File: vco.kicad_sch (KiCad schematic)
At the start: 122 parts, among them J1 EXP FM, J10 Square, J11 Conn_02x05_Odd_Even, J2 1V/OCT, J3 1V/OCT, J4 LIN FM, J5 PWM, J6 SYNC, J7 Sine, J8 Saw, J9 Triangle, Q1 MMBFJ111, SW1 Sync Mode, U1 TL074, U2 OPA2134, U3 L78L12_SO8, U4 L79L12_SO8, U5 thermally_coupled_transistor_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, U6 TL074, U7 LM311

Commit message: checking all resistor values
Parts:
- RV11: value 220K -> 47K
- RV9: value 220K -> 10K
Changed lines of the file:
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@@
     (in_bom yes) (on_board yes) (fields_autoplaced)
     (property "Reference" "RV9" (id 0) (at 182.88 119.8864 90))
-    (property "Value" "220K" (id 1) (at 182.88 122.4233 90))
+    (property "Value" "10K" (id 1) (at 182.88 122.4233 90))
     (property "Footprint" "Potentiometer_THT:Potentiometer_Bourns_3296W_Vertical" (id 2) (at 182.88 116.84 0)
       (effects (font (size 1.27 1.27)) hide)
@@
     (in_bom yes) (on_board yes) (fields_autoplaced)
     (property "Reference" "RV11" (id 0) (at 265.43 13.0642 90))
-    (property "Value" "220K" (id 1) (at 265.43 15.6011 90))
+    (property "Value" "47K" (id 1) (at 265.43 15.6011 90))
     (property "Footprint" "Potentiometer_THT:Potentiometer_Bourns_3296W_Vertical" (id 2) (at 265.43 17.78 0)
       (effects (font (size 1.27 1.27)) hide)
@@
     )
     (path "/58d5e9aa-5595-4f3e-9fc6-52cb927712d1"
-      (reference "RV9") (unit 1) (value "220K") (footprint "Potentiometer_THT:Potentiometer_Bourns_3296W_Vertical")
+      (reference "RV9") (unit 1) (value "10K") (footprint "Potentiometer_THT:Potentiometer_Bourns_3296W_Vertical")
     )
     (path "/37fdaf0a-cf60-456d-b11f-b915c1ec581e"
@@
     )
     (path "/a99e6af1-8dcb-42e4-b924-4b2e7e354e65"
-      (reference "RV11") (unit 1) (value "220K") (footprint "Potentiometer_THT:Potentiometer_Bourns_3296W_Vertical")
+      (reference "RV11") (unit 1) (value "47K") (footprint "Potentiometer_THT:Potentiometer_Bourns_3296W_Vertical")
     )
     (path "/a04003e4-c542-4884-a43e-7ae3c8ee89d5"

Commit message: v2 ready for manu
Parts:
- added D7, D8: D_Dual_Series_AKC, Package_TO_SOT_SMD:SOT-23_Handsoldering, symbol Device:D_Dual_Series_AKC
- D1, D2, D3, D4, D5, D6: footprint Diode_SMD:D_SOD-323 -> Diode_SMD:D_SOD-323_HandSoldering
- H1: value 1V/OCT -> 1v/oct; symbol Mechanical:MountingHole -> Mechanical:MountingHole_Pad; now left out of the parts list
- H10: value MountingHole -> square; footprint (none) -> Eurorack:Mech-AudioJack-Hole-Output; symbol Mechanical:MountingHole -> Eurorack:MountingHole_Pad_Output; now left out of the parts list
- H11: value MountingHole -> frequency; footprint (none) -> Eurorack:Mech-Potentiometer-Hole_level; symbol Mechanical:MountingHole -> Mechanical:MountingHole_Pad; now left out of the parts list
- H12: value MountingHole -> fine tune; footprint (none) -> Eurorack:Mech-Potentiometer-Hole_pan; symbol Mechanical:MountingHole -> Mechanical:MountingHole_Pad; now left out of the parts list
- H13: value MountingHole -> lin fm; footprint (none) -> Eurorack:Mech-Potentiometer-Hole_level; symbol Mechanical:MountingHole -> Mechanical:MountingHole_Pad; now left out of the parts list
- H14: value MountingHole -> exp fm; footprint (none) -> Eurorack:Mech-Potentiometer-Hole_level; symbol Mechanical:MountingHole -> Mechanical:MountingHole_Pad; now left out of the parts list
- H15: value MountingHole -> pw; footprint (none) -> Eurorack:Mech-Potentiometer-Hole_pan; symbol Mechanical:MountingHole -> Mechanical:MountingHole_Pad; now left out of the parts list
- H16: value MountingHole -> pwm lvl; footprint (none) -> Eurorack:Mech-Potentiometer-Hole_level; symbol Mechanical:MountingHole -> Mechanical:MountingHole_Pad; now left out of the parts list
- H17: footprint (none) -> Eurorack:Mech-MountingHole; symbol Mechanical:MountingHole -> Mechanical:MountingHole_Pad; now left out of the parts list
- H18, H19, H20: symbol Mechanical:MountingHole -> Mechanical:MountingHole_Pad; now left out of the parts list
- H2: value MountingHole -> 1v/oct; footprint (none) -> Eurorack:Mech-AudioJack-Hole; symbol Mechanical:MountingHole -> Mechanical:MountingHole_Pad; now left out of the parts list
- H21: value MountingHole -> sync hardness; footprint (none) -> Eurorack:Mech-2M_Switch-Hole; symbol Mechanical:MountingHole -> Mechanical:MountingHole_Pad; now left out of the parts list
- H3: value MountingHole -> exp fm; footprint (none) -> Eurorack:Mech-AudioJack-Hole; symbol Mechanical:MountingHole -> Mechanical:MountingHole_Pad; now left out of the parts list
- H4: value MountingHole -> lin fm; footprint (none) -> Eurorack:Mech-AudioJack-Hole; symbol Mechanical:MountingHole -> Mechanical:MountingHole_Pad; now left out of the parts list
- H5: value MountingHole -> pwm; footprint (none) -> Eurorack:Mech-AudioJack-Hole; symbol Mechanical:MountingHole -> Mechanical:MountingHole_Pad; now left out of the parts list
- H6: value MountingHole -> sync; footprint (none) -> Eurorack:Mech-AudioJack-Hole; symbol Mechanical:MountingHole -> Mechanical:MountingHole_Pad; now left out of the parts list
- H7: value MountingHole -> sine; footprint (none) -> Eurorack:Mech-AudioJack-Hole-Output; symbol Mechanical:MountingHole -> Mechanical:MountingHole_Pad; now left out of the parts list
- H8: value MountingHole -> triangle; footprint (none) -> Eurorack:Mech-AudioJack-Hole-Output; symbol Mechanical:MountingHole -> Mechanical:MountingHole_Pad; now left out of the parts list
- H9: value MountingHole -> saw; footprint (none) -> Eurorack:Mech-AudioJack-Hole-Output; symbol Mechanical:MountingHole -> Mechanical:MountingHole_Pad; now left out of the parts list
- J1, J10, J2, J3, J4, J5, J6, J7, J8, J9: symbol Connector:AudioJack2_SwitchT -> Connector_Audio:AudioJack2_SwitchT; PartNum (none) -> A-2566; Vendor (none) -> Tayda
- J11: PartNum (none) -> A-2939; Vendor (none) -> Tayda
- Q1: PartNum (none) -> 512-MMBFJ111; Vendor (none) -> Mouser
- RV1: value EXP FM LVL -> B25K; PartNum (none) -> A-2491; Vendor (none) -> Tayda
- RV10: PartNum (none) -> A-587; Vendor (none) -> Tayda
- RV11: PartNum (none) -> A-598; Vendor (none) -> Tayda
- RV2: value LIN FM LVL -> B25K; PartNum (none) -> A-2491; Vendor (none) -> Tayda
- RV3: value PWM LVL -> B25K; PartNum (none) -> A-2491; Vendor (none) -> Tayda
- RV4: value Tune -> B25K; PartNum (none) -> A-2491; Vendor (none) -> Tayda
- RV5: value Fine Tune -> B25K; PartNum (none) -> A-2491; Vendor (none) -> Tayda
- RV6: PartNum (none) -> A-310; Vendor (none) -> Tayda
- RV7: value PW -> B25K; PartNum (none) -> A-2491; Vendor (none) -> Tayda
- RV8: PartNum (none) -> A-595; Vendor (none) -> Tayda
- RV9: PartNum (none) -> A-586; Vendor (none) -> Tayda
- SW1: PartNum (none) -> X-4673; Vendor (none) -> Tayda
- U1: PartNum (none) -> 595-TL074CN; Vendor (none) -> Mouser
- U2: PartNum (none) -> 595-OPA2137UA/2K5 --or-- 595-OPA2134UA/2K5; Vendor (none) -> Mouser
- U3: PartNum (none) -> 863-NCV78L12ABDR2G; Vendor (none) -> Mouser
- U4: PartNum (none) -> 863-MC79L12ABDR2G; Vendor (none) -> Mouser
- U5: PartNum (none) -> 771-BCM847DS135 --and-- LT16S102F33; Vendor (none) -> Mouser --and-- Thonk
- U6: PartNum (none) -> 595-TL074CDR; Vendor (none) -> Mouser
- U7: PartNum (none) -> 863-LM311DR2G; Vendor (none) -> Mouser
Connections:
- net GND: now also U6.12 (+); no longer U1.12 (+)
- net at D3.1 (K), R30.1, R35.1: now also U6.13 (-); no longer U1.13 (-)
- net at R12.2, U3.8 (IN): now also D7.2 (K), D8.2 (K); no longer J11.10 (Pin_10), J11.9 (Pin_9)
- net at R31.2, R32.2, R34.2: now also U1.12 (+); no longer U6.12 (+)
- net at R33.1: now also U1.13 (-); no longer U6.13 (-)
- net at U6.14: now also D3.2 (A), D4.1 (K); no longer R39.2
- net at R13.1, U4.2 (IN), U4.3 (IN)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: now also D7.1 (A), D8.1 (A); no longer J11.1 (Pin_1), J11.2 (Pin_2)
- new net: D8.3 (common), J11.1 (Pin_1), J11.2 (Pin_2)
- new net: D7.3 (common), J11.10 (Pin_10), J11.9 (Pin_9)
- new net: R39.2, U1.14
- new net face: H1.1, H10.1, H11.1, H12.1, H13.1, H14.1, H15.1, H16.1, H17.1, H18.1, H19.1, H2.1, H20.1, H21.1, H3.1, H4.1, H5.1, H6.1, H7.1, H8.1, H9.1
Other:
- moved on the sheet: D6, J11, U1D, U6D

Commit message: wrong part number
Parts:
- SW1: PartNum X-4673 -> A-6087
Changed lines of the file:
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@@
       (effects (font (size 1.27 1.27)) hide)
     )
-    (property "PartNum" "X-4673" (at 52.07 116.84 0)
+    (property "PartNum" "A-6087" (at 52.07 116.84 0)
       (effects (font (size 1.27 1.27)) hide)
     )

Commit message: v2 just about ready for manu
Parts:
- D7, D8: footprint Package_TO_SOT_SMD:SOT-23_Handsoldering -> Package_TO_SOT_SMD:SOT-23
- H1, H2: footprint Eurorack:Mech-AudioJack-Hole -> Eurorack:Mech-AudioJack-Hole-Input-Voct
- H3, H4, H5: footprint Eurorack:Mech-AudioJack-Hole -> Eurorack:Mech-AudioJack-Hole-Input-CV
- H6: footprint Eurorack:Mech-AudioJack-Hole -> Eurorack:Mech-AudioJack-Hole-Input-Clock
- Q1: value MMBFJ111 -> MMBFJ113
- R40: value 4.7K -> 8.2K
- R45: value 200K -> 180K
- R49: value 1.5K -> 1.2K
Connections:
- net +12V: now also D7.2 (K), D8.2 (K), U3.8 (IN); no longer R12.1
- net -12V: now also D7.1 (A), D8.1 (A), U4.2 (IN), U4.3 (IN), U4.6 (IN), U4.7 (IN); no longer R13.2
- net at J11.1 (Pin_1), J11.2 (Pin_2): now also R13.2; no longer D8.3 (common)
- net at J11.10 (Pin_10), J11.9 (Pin_9): now also R12.1; no longer D7.3 (common)
- new net: D8.3 (common), R13.1
- new net: D7.3 (common), R12.2
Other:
- moved on the sheet: C10, C8, C9, R12, R13, U1E, U2C, U6E

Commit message: bom fixes
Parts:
- C2, C3: value 22U 50V -> 22u 50V
- R1: value 70K -> 68K
- R2, R38: value 50K -> 47K
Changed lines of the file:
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@@
   (symbol (lib_id "Device:C") (at 116.84 238.76 90) (unit 1)
     (in_bom yes) (on_board yes) (dnp no) (fields_autoplaced)
-    (property "Reference" "C3" (at 116.84 232.9012 90)
+    (property "Reference" "C3" (at 116.84 231.14 90)
       (effects (font (size 1.27 1.27)))
     )
-    (property "Value" "22U 50V" (at 116.84 235.4381 90)
+    (property "Value" "22u 50V" (at 116.84 233.68 90)
       (effects (font (size 1.27 1.27)))
     )
@@
   (symbol (lib_id "Device:R") (at 254 39.37 0) (unit 1)
     (in_bom yes) (on_board yes) (dnp no) (fields_autoplaced)
-    (property "Reference" "R38" (at 255.778 38.5353 0)
+    (property "Reference" "R38" (at 256.54 38.1 0)
       (effects (font (size 1.27 1.27)) (justify left))
     )
-    (property "Value" "50K" (at 255.778 41.0722 0)
+    (property "Value" "47K" (at 256.54 40.64 0)
       (effects (font (size 1.27 1.27)) (justify left))
     )
@@
   (symbol (lib_id "Device:C") (at 116.84 209.55 90) (unit 1)
     (in_bom yes) (on_board yes) (dnp no) (fields_autoplaced)
-    (property "Reference" "C2" (at 116.84 203.6912 90)
+    (property "Reference" "C2" (at 116.84 201.93 90)
       (effects (font (size 1.27 1.27)))
     )
-    (property "Value" "22U 50V" (at 116.84 206.2281 90)
+    (property "Value" "22u 50V" (at 116.84 204.47 90)
       (effects (font (size 1.27 1.27)))
     )
@@
   (symbol (lib_id "Device:R") (at 87.63 41.91 180) (unit 1)
     (in_bom yes) (on_board yes) (dnp no) (fields_autoplaced)
-    (property "Reference" "R1" (at 89.408 41.0753 0)
+    (property "Reference" "R1" (at 90.17 40.64 0)
       (effects (font (size 1.27 1.27)) (justify right))
     )
-    (property "Value" "70K" (at 89.408 43.6122 0)
+    (property "Value" "68K" (at 90.17 43.18 0)
       (effects (font (size 1.27 1.27)) (justify right))
     )
@@
   (symbol (lib_id "Device:R") (at 87.63 49.53 180) (unit 1)
     (in_bom yes) (on_board yes) (dnp no) (fields_autoplaced)
-    (property "Reference" "R2" (at 89.408 48.6953 0)
+    (property "Reference" "R2" (at 90.17 48.26 0)
       (effects (font (size 1.27 1.27)) (justify right))
     )
-    (property "Value" "50K" (at 89.408 51.2322 0)
+    (property "Value" "47K" (at 90.17 50.8 0)
       (effects (font (size 1.27 1.27)) (justify right))
     )

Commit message: more bom fixes
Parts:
- SW1: PartNum A-6087 -> A-5751
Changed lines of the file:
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@@
       (effects (font (size 1.27 1.27)) hide)
     )
-    (property "PartNum" "A-6087" (at 52.07 116.84 0)
+    (property "PartNum" "A-5751" (at 52.07 116.84 0)
       (effects (font (size 1.27 1.27)) hide)
     )

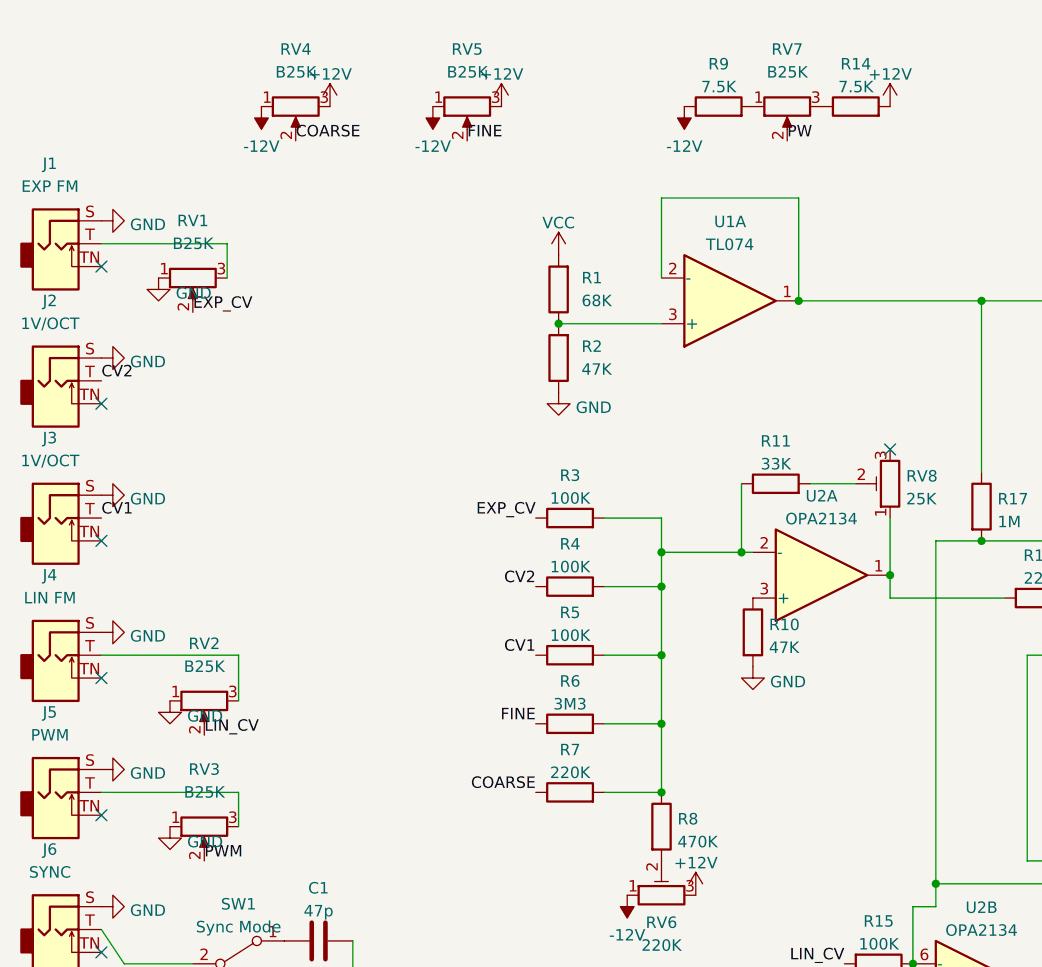
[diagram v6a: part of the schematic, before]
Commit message: more BOM fixes
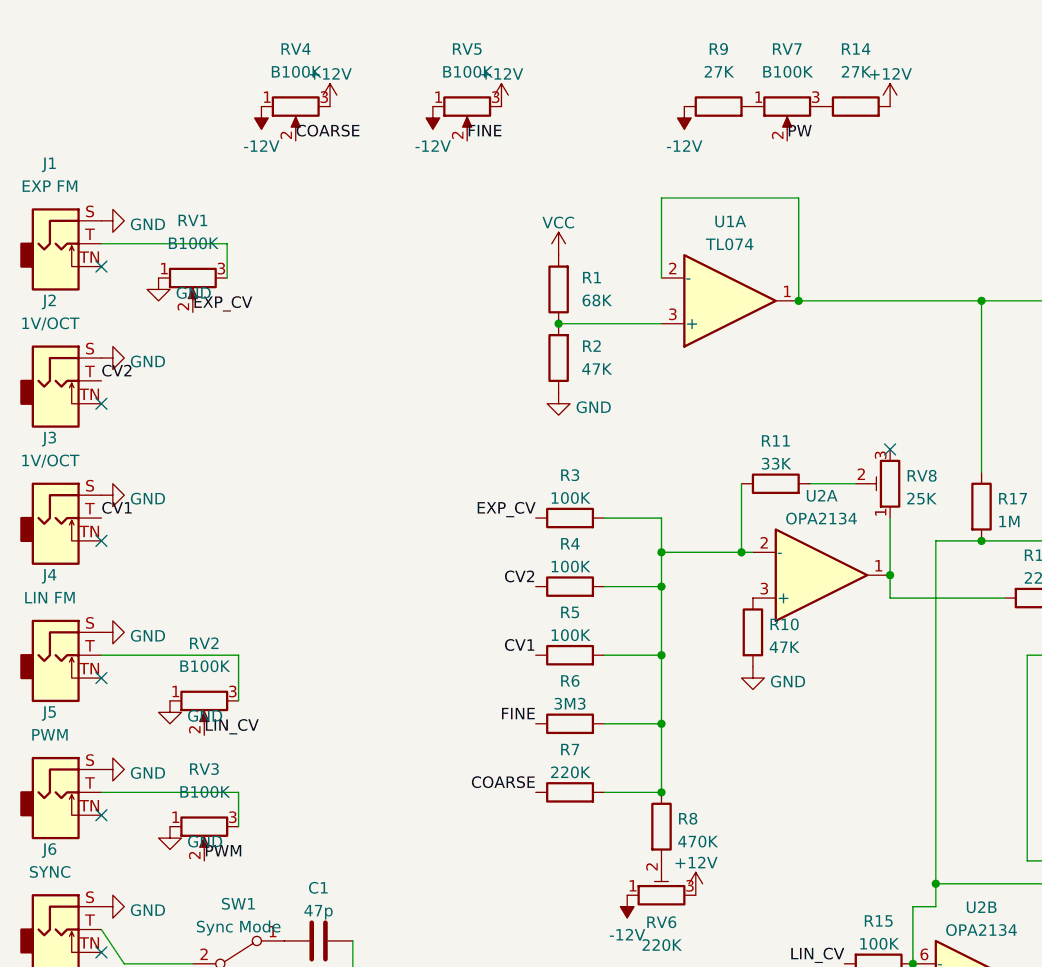
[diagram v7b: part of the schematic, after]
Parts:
- Q1: PartNum 512-MMBFJ111 -> 512-MMBFJ113
- R14, R9: value 7.5K -> 27K
- RV1, RV2, RV3, RV4, RV5, RV7: value B25K -> B100K
- U1: PartNum 595-TL074CN -> 595-TL074CDR
- U2: PartNum 595-OPA2137UA/2K5 --or-- 595-OPA2134UA/2K5 -> 595-OPA2134UA/2K5
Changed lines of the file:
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@@
       (effects (font (size 1.27 1.27)) hide)
     )
-    (property "PartNum" "595-TL074CN" (at 374.65 233.68 0)
+    (property "PartNum" "595-TL074CDR" (at 374.65 233.68 0)
       (effects (font (size 1.27 1.27)) hide)
     )
@@
       (effects (font (size 1.27 1.27)) hide)
     )
-    (property "PartNum" "595-OPA2137UA/2K5 --or-- 595-OPA2134UA/2K5" (at 116.84 73.66 0)
+    (property "PartNum" "595-OPA2134UA/2K5" (at 116.84 73.66 0)
       (effects (font (size 1.27 1.27)) hide)
     )
@@
   (symbol (lib_id "Device:R") (at 105.41 21.59 90) (unit 1)
     (in_bom yes) (on_board yes) (dnp no) (fields_autoplaced)
-    (property "Reference" "R9" (at 105.41 16.8742 90)
+    (property "Reference" "R9" (at 105.41 15.24 90)
       (effects (font (size 1.27 1.27)))
     )
-    (property "Value" "7.5K" (at 105.41 19.4111 90)
+    (property "Value" "27K" (at 105.41 17.78 90)
       (effects (font (size 1.27 1.27)))
     )
@@
       (effects (font (size 1.27 1.27)) hide)
     )
-    (property "PartNum" "595-TL074CN" (at 246.38 105.41 0)
+    (property "PartNum" "595-TL074CDR" (at 246.38 105.41 0)
       (effects (font (size 1.27 1.27)) hide)
     )
@@
       (effects (font (size 1.27 1.27)))
     )
-    (property "Value" "B25K" (at 48.26 83.82 90)
+    (property "Value" "B100K" (at 48.26 83.82 90)
       (effects (font (size 1.27 1.27)))
     )
@@
       (effects (font (size 1.27 1.27)))
     )
-    (property "Value" "B25K" (at 77.47 17.78 90)
+    (property "Value" "B100K" (at 77.47 17.78 90)
       (effects (font (size 1.27 1.27)))
     )
@@
       (effects (font (size 1.27 1.27)) hide)
     )
-    (property "PartNum" "595-OPA2137UA/2K5 --or-- 595-OPA2134UA/2K5" (at 134.62 119.38 0)
+    (property "PartNum" "595-OPA2134UA/2K5" (at 134.62 119.38 0)
       (effects (font (size 1.27 1.27)) hide)
     )
@@
   (symbol (lib_id "Device:R") (at 120.65 21.59 90) (unit 1)
     (in_bom yes) (on_board yes) (dnp no) (fields_autoplaced)
-    (property "Reference" "R14" (at 120.65 16.8742 90)
+    (property "Reference" "R14" (at 120.65 15.24 90)
       (effects (font (size 1.27 1.27)))
     )
-    (property "Value" "7.5K" (at 120.65 19.4111 90)
+    (property "Value" "27K" (at 120.65 17.78 90)
       (effects (font (size 1.27 1.27)))
     )
@@
       (effects (font (size 1.27 1.27)))
     )
-    (property "Value" "B25K" (at 46.99 36.83 90)
+    (property "Value" "B100K" (at 46.99 36.83 90)
       (effects (font (size 1.27 1.27)))
     )
@@
       (effects (font (size 1.27 1.27)) hide)
     )
-    (property "PartNum" "595-OPA2137UA/2K5 --or-- 595-OPA2134UA/2K5" (at 346.71 233.68 0)
+    (property "PartNum" "595-OPA2134UA/2K5" (at 346.71 233.68 0)
       (effects (font (size 1.27 1.27)) hide)
     )
@@
       (effects (font (size 1.27 1.27)))
     )
-    (property "Value" "B25K" (at 48.26 97.79 90)
+    (property "Value" "B100K" (at 48.26 97.79 90)
       (effects (font (size 1.27 1.27)))
     )
@@
       (effects (font (size 1.27 1.27)) hide)
     )
-    (property "PartNum" "595-TL074CN" (at 106.68 43.18 0)
+    (property "PartNum" "595-TL074CDR" (at 106.68 43.18 0)
       (effects (font (size 1.27 1.27)) hide)
     )
@@
       (effects (font (size 1.27 1.27)))
     )
-    (property "Value" "B25K" (at 113.03 17.78 90)
+    (property "Value" "B100K" (at 113.03 17.78 90)
       (effects (font (size 1.27 1.27)))
     )
@@
       (effects (font (size 1.27 1.27)) hide)
     )
-    (property "PartNum" "595-TL074CN" (at 179.07 71.12 0)
+    (property "PartNum" "595-TL074CDR" (at 179.07 71.12 0)
       (effects (font (size 1.27 1.27)) hide)
     )
@@
       (effects (font (size 1.27 1.27)) hide)
     )
-    (property "PartNum" "512-MMBFJ111" (at 167.64 55.88 0)
+    (property "PartNum" "512-MMBFJ113" (at 167.64 55.88 0)
       (effects (font (size 1.27 1.27)) hide)
     )
@@
       (effects (font (size 1.27 1.27)))
     )
-    (property "Value" "B25K" (at 58.42 17.78 90)
+    (property "Value" "B100K" (at 58.42 17.78 90)
       (effects (font (size 1.27 1.27)))
     )
@@
       (effects (font (size 1.27 1.27)) hide)
     )
-    (property "PartNum" "595-TL074CN" (at 201.93 102.87 0)
+    (property "PartNum" "595-TL074CDR" (at 201.93 102.87 0)
       (effects (font (size 1.27 1.27)) hide)
     )

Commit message: use bigger potentiometers (i've got some)
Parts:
- RV1, RV2, RV3, RV4, RV5, RV7: PartNum A-2491 -> A-2963
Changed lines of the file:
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@@
       (effects (font (size 1.27 1.27)) hide)
     )
-    (property "PartNum" "A-2491" (at 48.26 87.63 90)
+    (property "PartNum" "A-2963" (at 48.26 87.63 90)
       (effects (font (size 1.27 1.27)) hide)
     )
@@
       (effects (font (size 1.27 1.27)) hide)
     )
-    (property "PartNum" "A-2491" (at 77.47 21.59 90)
+    (property "PartNum" "A-2963" (at 77.47 21.59 90)
       (effects (font (size 1.27 1.27)) hide)
     )
@@
       (effects (font (size 1.27 1.27)) hide)
     )
-    (property "PartNum" "A-2491" (at 46.99 40.64 90)
+    (property "PartNum" "A-2963" (at 46.99 40.64 90)
       (effects (font (size 1.27 1.27)) hide)
     )
@@
       (effects (font (size 1.27 1.27)) hide)
     )
-    (property "PartNum" "A-2491" (at 48.26 101.6 90)
+    (property "PartNum" "A-2963" (at 48.26 101.6 90)
       (effects (font (size 1.27 1.27)) hide)
     )
@@
       (effects (font (size 1.27 1.27)) hide)
     )
-    (property "PartNum" "A-2491" (at 113.03 21.59 90)
+    (property "PartNum" "A-2963" (at 113.03 21.59 90)
       (effects (font (size 1.27 1.27)) hide)
     )
@@
       (effects (font (size 1.27 1.27)) hide)
     )
-    (property "PartNum" "A-2491" (at 58.42 21.59 90)
+    (property "PartNum" "A-2963" (at 58.42 21.59 90)
       (effects (font (size 1.27 1.27)) hide)
     )
